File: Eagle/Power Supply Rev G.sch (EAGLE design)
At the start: 19 parts, among them J1 694106301002, J2 61300211121, J4 61300211121, J5 61300211121, U1 LM317

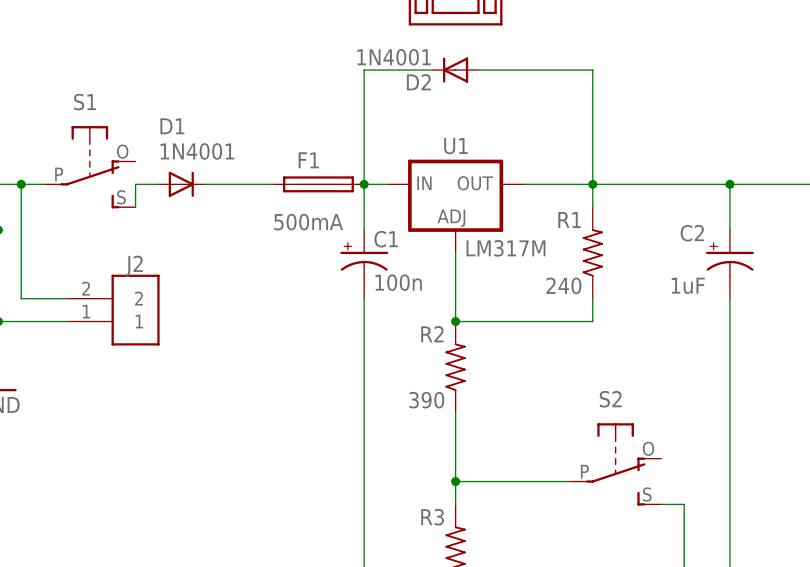
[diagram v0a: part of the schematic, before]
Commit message: changes to BOM for manufacturing
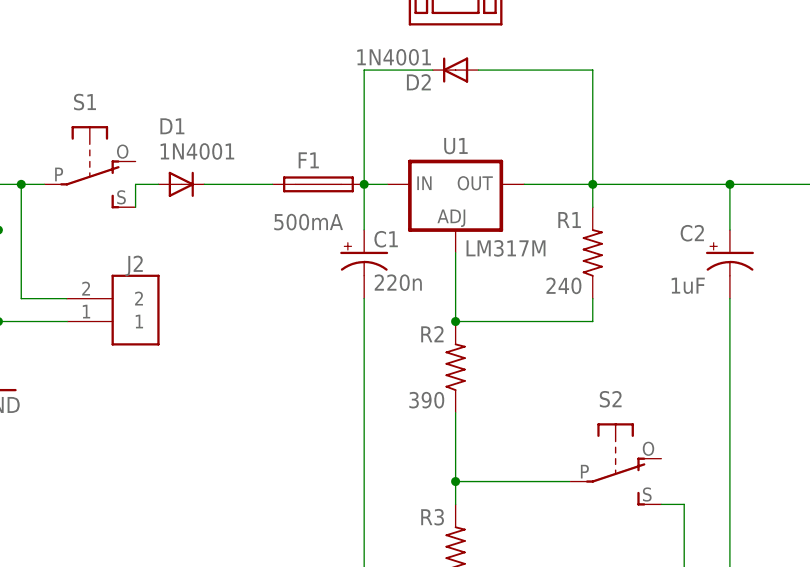
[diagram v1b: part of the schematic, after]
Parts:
- C1: value 100n -> 220n
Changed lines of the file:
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@@
 <part name="R1" library="Quantum Projects" library_urn="urn:adsk.eagle:library:19630877" deviceset="RESISTOR" device="" package3d_urn="urn:adsk.eagle:package:21713525/3" value="240"/>
 <part name="C2" library="Quantum Projects" library_urn="urn:adsk.eagle:library:19630877" deviceset="E-CAPACITOR" device="2-4" package3d_urn="urn:adsk.eagle:package:21734552/2" value="1uF"/>
-<part name="C1" library="Quantum Projects" library_urn="urn:adsk.eagle:library:19630877" deviceset="E-CAPACITOR" device="2-4" package3d_urn="urn:adsk.eagle:package:21734552/2" value="100n"/>
+<part name="C1" library="Quantum Projects" library_urn="urn:adsk.eagle:library:19630877" deviceset="E-CAPACITOR" device="2-4" package3d_urn="urn:adsk.eagle:package:21734552/2" value="220n"/>
 <part name="D1" library="Quantum Projects" library_urn="urn:adsk.eagle:library:19630877" deviceset="1N4000" device="" package3d_urn="urn:adsk.eagle:package:20494835/2" value="1N4001"/>
 <part name="R2" library="Quantum Projects" library_urn="urn:adsk.eagle:library:19630877" deviceset="RESISTOR" device="" package3d_urn="urn:adsk.eagle:package:21713525/3" value="390"/>
